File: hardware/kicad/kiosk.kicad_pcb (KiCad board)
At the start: 2 copper layers, 158 x 121 mm, 20 parts, among them J10 TerminalBlock_MaiXu_MX126-5.0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, J11 TerminalBlock_MaiXu_MX126-5.0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, J13 PinHeader_1x09_P2.54mm_Vertic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, J14 PinHeader_1x04_P2.54mm_Vertic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, J3 PinSocket_1x14_P2.54mm_Vertic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, J4 PinSocket_1x06_P2.54mm_Vertic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, J5 PinSocket_1x04_P2.54mm_Vertic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, J6 PinSocket_1x06_P2.54mm_Vertic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, J7 PinSocket_1x07_P2.54mm_Vertic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, J9 PinHeader_1x03_P2.54mm_Vertic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, U1 ESP32-S3-CAM

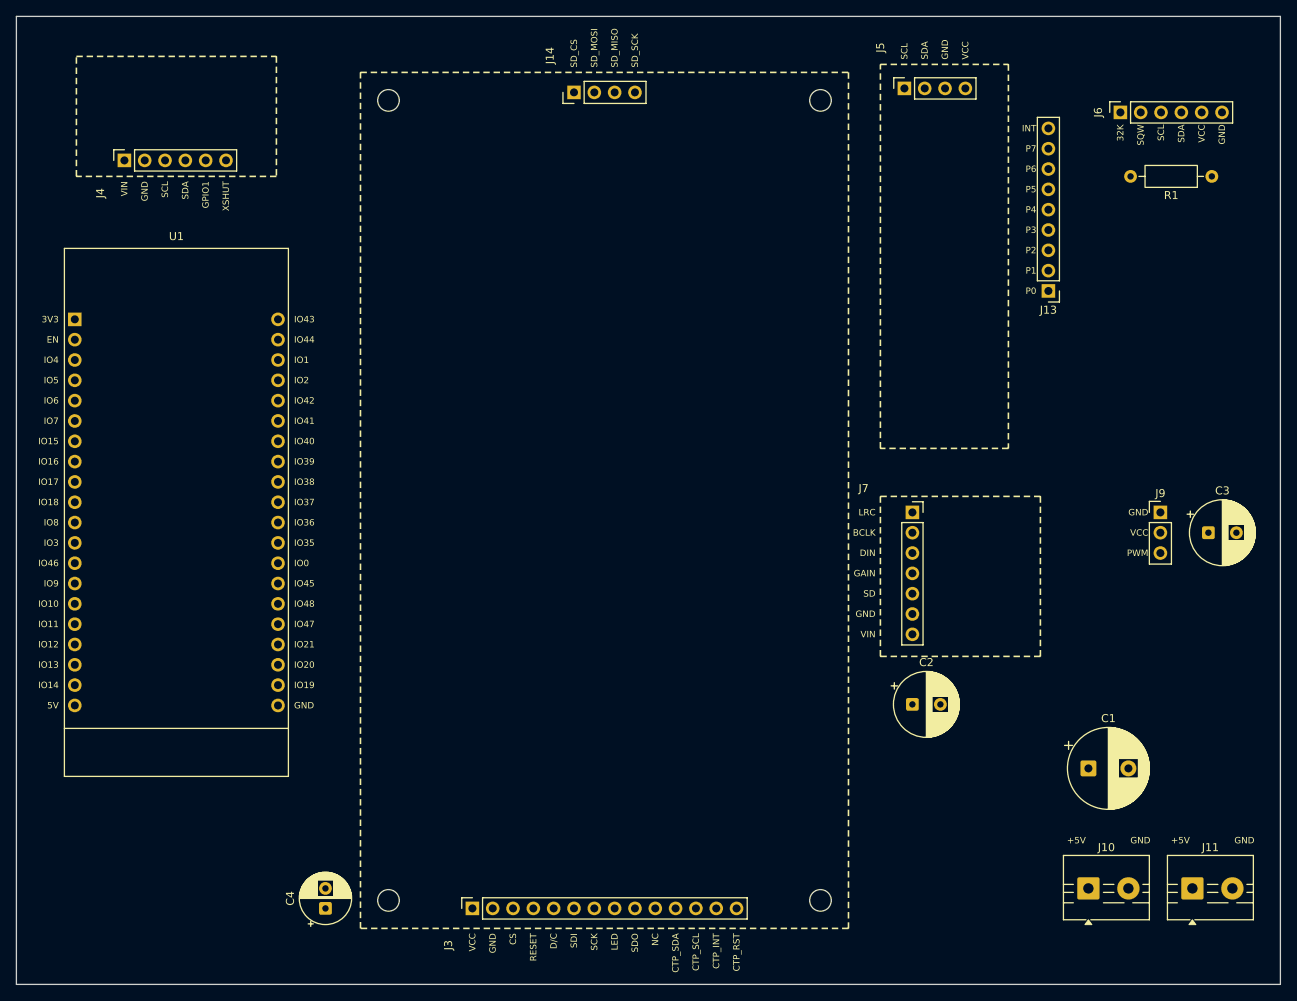
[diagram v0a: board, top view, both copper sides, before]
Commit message: fix(hardware): centre each socket across the module body it carries
J5's four-pin row sat 1.19 mm left of its outline's centre, so the
expander would have hung over one side of its own socket. J4 and J7 were
out by 0.15 and 0.38 for the same reason: the placements were typed to
land near the body rather than measured against it.

All four sockets under a module body are now centred along the axis their
row runs — J3 and J14 already were, because the panel rectangle is derived
from J3 rather than written down.

check_pcb gains the rule at a 0.3 mm tolerance, which is roughly where the
drift starts being visible against the dashed outline. Proven by putting
J5 back and watching it report -1.19.

Task: E14-T8
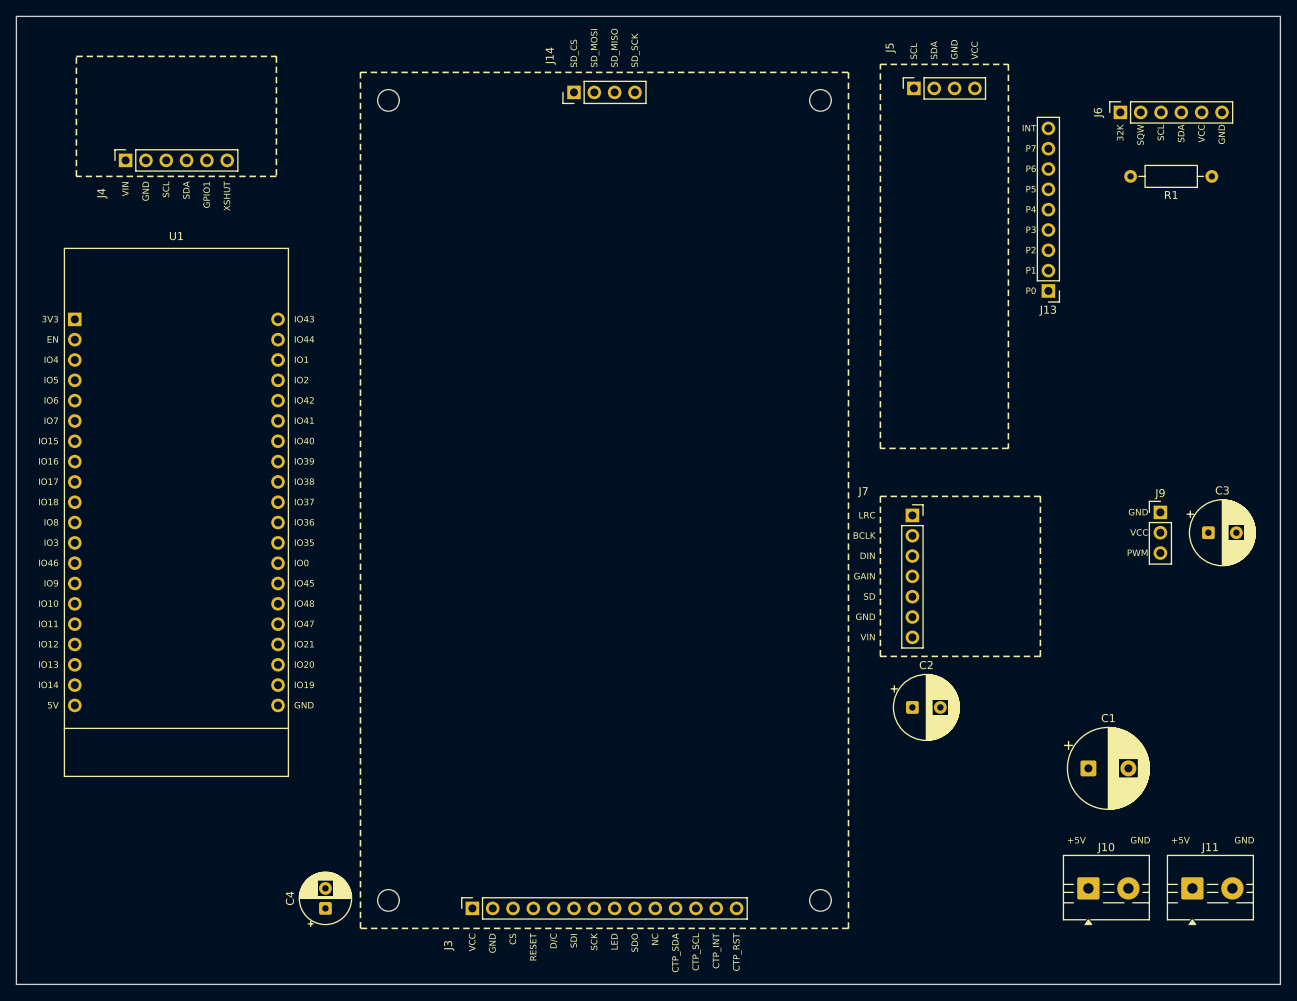
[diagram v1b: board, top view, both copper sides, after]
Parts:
- moved J5 1.19 mm to (112.2, 9.00)
- moved J7 0.38 mm to (112.0, 62.4)
- moved C2 0.38 mm to (112.0, 86.4)
- moved J4 0.15 mm to (13.7, 18.0)
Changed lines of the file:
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@@
 	(footprint "Connector_PinSocket_2.54mm:PinSocket_1x07_P2.54mm_Vertical"
 		(layer "F.Cu")
-		(at 112 62)
+		(at 112 62.38)
 		(descr "Through hole straight socket strip, 1x07, 2.54mm pitch, single row (from Kicad 4.0.7), script generated")
 		(tags "Through hole socket strip THT 1x07 2.54mm single row")
@@
 	(footprint "Connector_PinSocket_2.54mm:PinSocket_1x04_P2.54mm_Vertical"
 		(layer "F.Cu")
-		(at 111 9 90)
+		(at 112.19 9 90)
 		(descr "Through hole straight socket strip, 1x04, 2.54mm pitch, single row (from Kicad 4.0.7), script generated")
 		(tags "Through hole socket strip THT 1x04 2.54mm single row")
@@
 	(footprint "Connector_PinSocket_2.54mm:PinSocket_1x06_P2.54mm_Vertical"
 		(layer "F.Cu")
-		(at 13.5 18 90)
+		(at 13.65 18 90)
 		(descr "Through hole straight socket strip, 1x06, 2.54mm pitch, single row (from Kicad 4.0.7), script generated")
 		(tags "Through hole socket strip THT 1x06 2.54mm single row")
@@
 	(footprint "Capacitor_THT:CP_Radial_D8.0mm_P3.50mm"
 		(layer "F.Cu")
-		(at 112 86)
+		(at 112 86.38)
 		(descr "CP, Radial series, Radial, pin pitch=3.50mm, diameter=8mm, height=12mm, Electrolytic Capacitor")
 		(tags "CP Radial series Radial pin pitch 3.50mm diameter 8mm height 12mm Electrolytic Capacitor")
@@
 	)
 	(gr_text "LRC"
-		(at 107.4 62 0)
+		(at 107.4 62.38 0)
 		(layer "F.SilkS")
 		(effects
@@
 	)
 	(gr_text "BCLK"
-		(at 107.4 64.54 0)
+		(at 107.4 64.92 0)
 		(layer "F.SilkS")
 		(effects
@@
 	)
 	(gr_text "DIN"
-		(at 107.4 67.08 0)
+		(at 107.4 67.46 0)
 		(layer "F.SilkS")
 		(effects
@@
 	)
 	(gr_text "GAIN"
-		(at 107.4 69.62 0)
+		(at 107.4 70 0)
 		(layer "F.SilkS")
 		(effects
@@
 	)
 	(gr_text "SD"
-		(at 107.4 72.16 0)
+		(at 107.4 72.54 0)
 		(layer "F.SilkS")
 		(effects
@@
 	)
 	(gr_text "GND"
-		(at 107.4 74.7 0)
+		(at 107.4 75.08 0)
 		(layer "F.SilkS")
 		(effects
@@
 	)
 	(gr_text "VIN"
-		(at 107.4 77.24 0)
+		(at 107.4 77.62 0)
 		(layer "F.SilkS")
 		(effects
@@
 	)
 	(gr_text "SCL"
-		(at 111 5.4 90)
+		(at 112.19 5.4 90)
 		(layer "F.SilkS")
 		(effects
@@
 	)
 	(gr_text "SDA"
-		(at 113.54 5.4 90)
+		(at 114.73 5.4 90)
 		(layer "F.SilkS")
 		(effects
@@
 	)
 	(gr_text "GND"
-		(at 116.08 5.4 90)
+		(at 117.27 5.4 90)
 		(layer "F.SilkS")
 		(effects
@@
 	)
 	(gr_text "VCC"
-		(at 118.62 5.4 90)
+		(at 119.81 5.4 90)
 		(layer "F.SilkS")
 		(effects
@@
 	)
 	(gr_text "VIN"
-		(at 13.5 20.6 90)
+		(at 13.65 20.6 90)
 		(layer "F.SilkS")
 		(effects
@@
 	)
 	(gr_text "GND"
-		(at 16.04 20.6 90)
+		(at 16.19 20.6 90)
 		(layer "F.SilkS")
 		(effects
@@
 	)
 	(gr_text "SCL"
-		(at 18.58 20.6 90)
+		(at 18.73 20.6 90)
 		(layer "F.SilkS")
 		(effects
@@
 	)
 	(gr_text "SDA"
-		(at 21.12 20.6 90)
+		(at 21.27 20.6 90)
 		(layer "F.SilkS")
 		(effects
@@
 	)
 	(gr_text "GPIO1"
-		(at 23.66 20.6 90)
+		(at 23.81 20.6 90)
 		(layer "F.SilkS")
 		(effects
@@
 	)
 	(gr_text "XSHUT"
-		(at 26.2 20.6 90)
+		(at 26.35 20.6 90)
 		(layer "F.SilkS")
 		(effects

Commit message: fix(hardware): set the three gaps around the panel equal
The panel sat 8.76 mm from the devkit and 3.99 mm from both the expander
and the amplifier outlines, so it read as pushed to the right of its own
row.

Halving the difference does not work: the left gap holds C4, whose can is
6.3 mm, and an even 6.38 mm gap leaves it 0.04 mm a side. So the panel
moves 1.46 mm left and the parts right of it move 1.85 mm right, which
lands all three gaps on 7.3 mm and keeps a quarter of a millimetre of
courtyard around the can. The board stays 158 wide because J9, C3, C1 and
the two terminals did not have to move with them.

The comment the previous commit added to gen_pcb.py used a word CI blocks
in comments; it is reworded here rather than left for the next run to trip
over.

Task: E14-T8
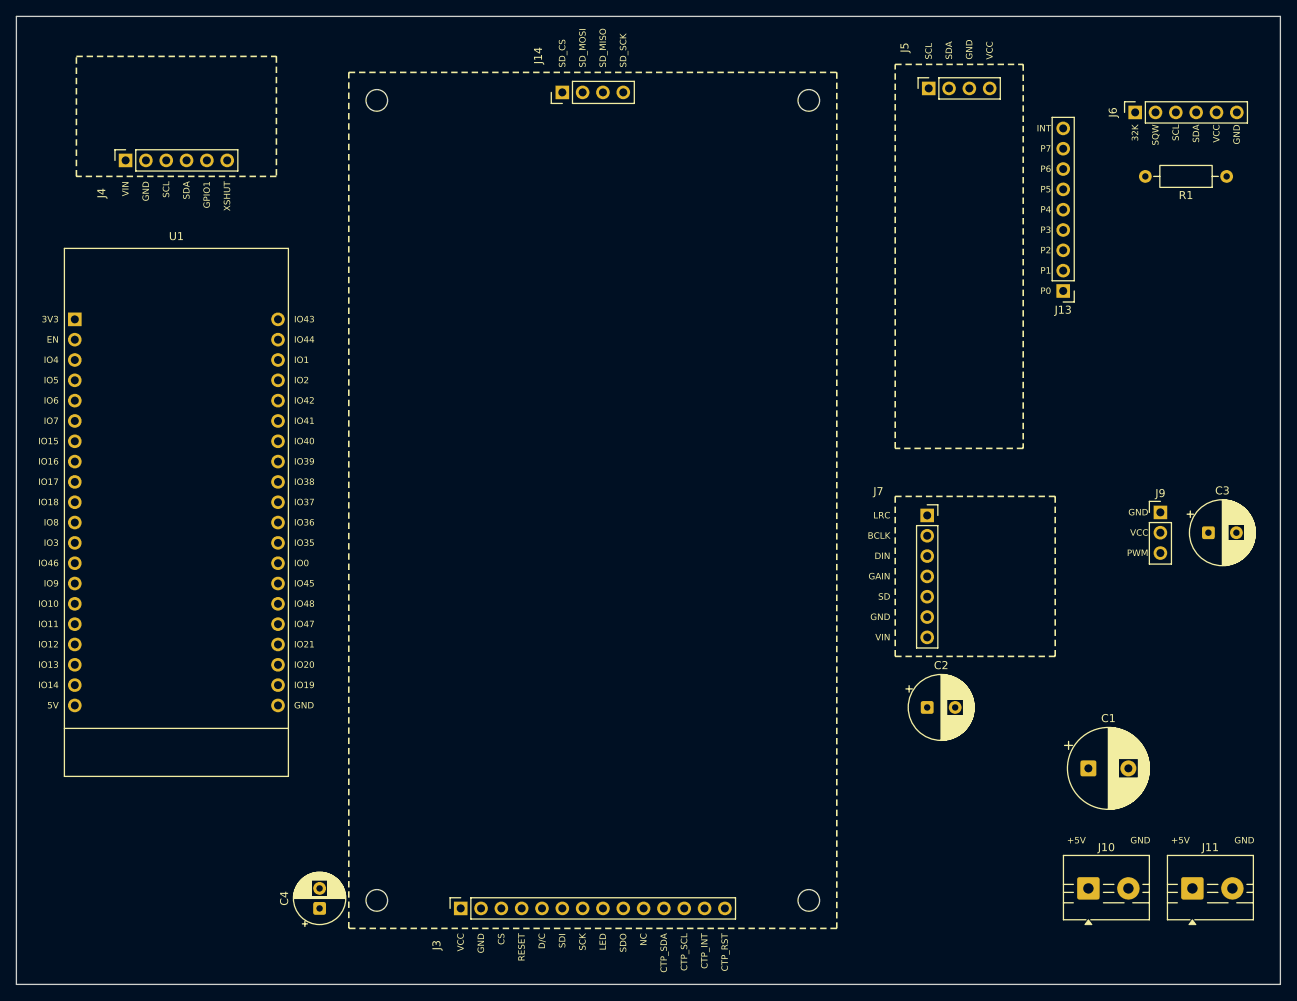
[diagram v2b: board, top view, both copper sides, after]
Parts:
- moved J5 1.85 mm to (114.0, 9.00)
- moved C2 1.85 mm to (113.8, 86.4)
- moved J13 1.85 mm to (130.8, 34.3)
- moved J6 1.85 mm to (139.8, 12.0)
- moved J7 1.85 mm to (113.8, 62.4)
- moved R1 1.85 mm to (151.3, 20.0)
- moved H2 1.46 mm to (99.0, 10.5)
- moved H3 1.46 mm to (99.0, 110.5)
- moved J14 1.46 mm to (68.2, 9.50)
- moved H1 1.46 mm to (45.0, 10.5)
- moved H4 1.46 mm to (45.0, 110.5)
- moved J3 1.46 mm to (55.5, 111.5)
- moved C4 0.73 mm to (37.9, 111.5)

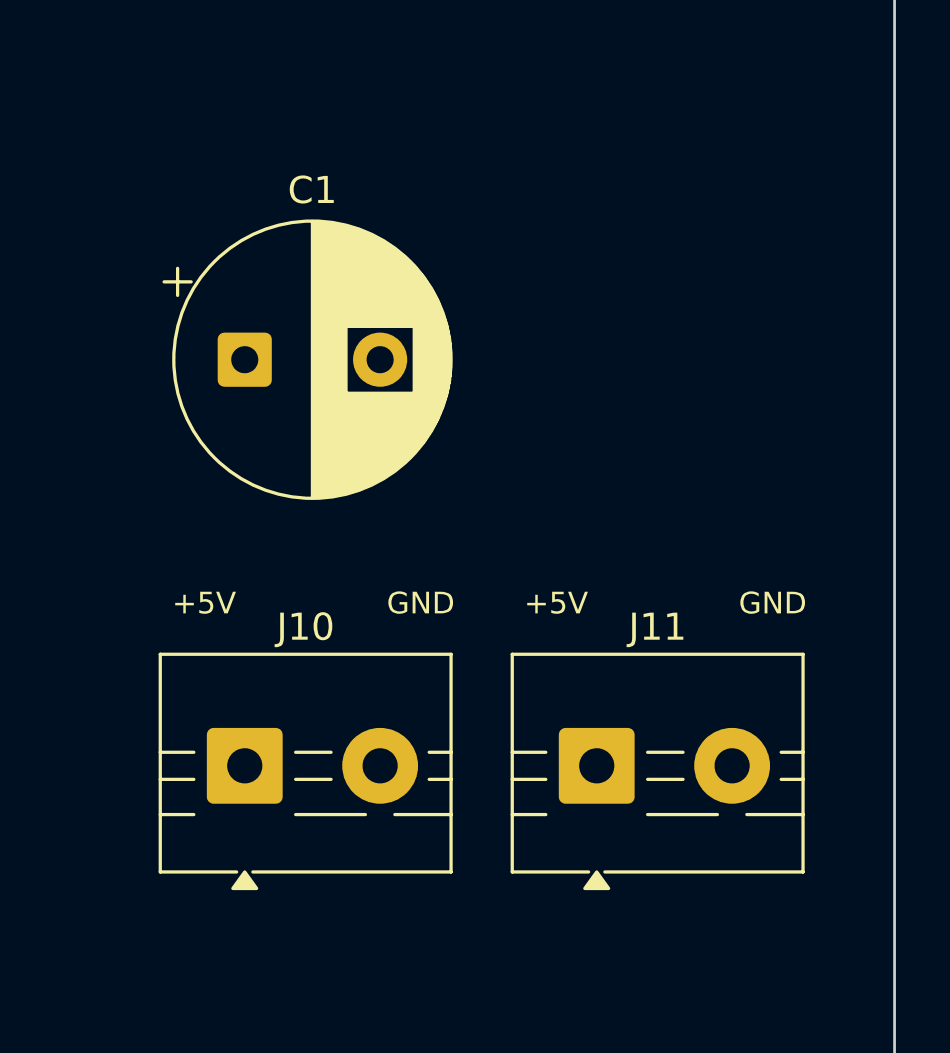
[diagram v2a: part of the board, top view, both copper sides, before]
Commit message: fix(hardware): put the two supply terminals in step and centre C1 on them
The four screws ran at 5.0, 8.0, 5.0 mm. The 8 was not a decision — it is
what was left when J11 moved inward to trim the board — and an uneven row
of identical terminals reads as a mistake. They now sit as close as their
courtyards allow, which is 6.5 mm, so the row goes 5.0, 6.5, 5.0 and the
two outlines touch rather than overlap.

That also makes rule 1 of section 2.5 nearly literal: J10.GND to J11.GND
is 11.5 mm, from 13.0.

C1 was aligned over J10 alone, leaving J11 outside the group. It is the
bulk store for the point where the two grounds meet, not for one terminal,
so it now centres across all four screws.

Task: E14-T8
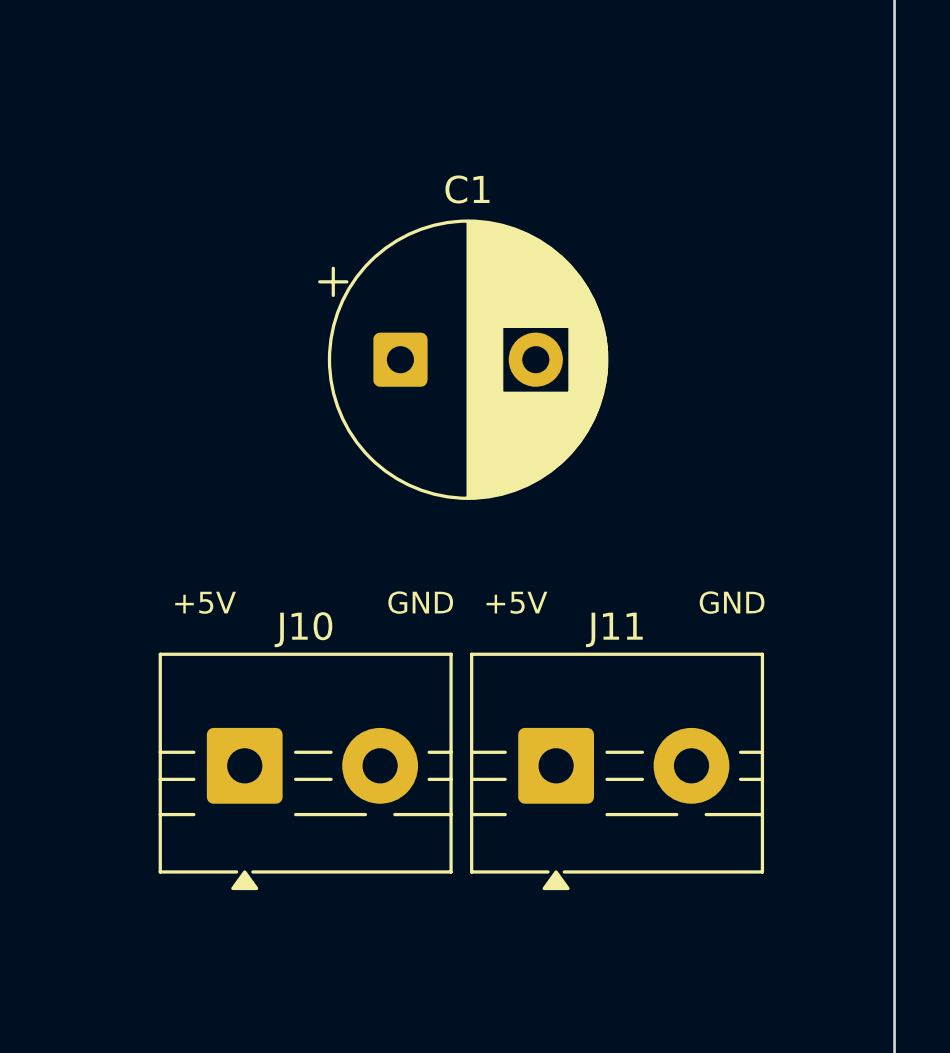
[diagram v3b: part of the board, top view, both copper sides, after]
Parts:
- moved C1 5.75 mm to (139.8, 94.0)
- moved J11 1.50 mm to (145.5, 109.0)
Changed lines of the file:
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@@
 	(footprint "TerminalBlock:TerminalBlock_MaiXu_MX126-5.0-02P_1x02_P5.00mm"
 		(layer "F.Cu")
-		(at 147 109)
+		(at 145.5 109)
 		(descr "terminal block MaiXu MX126-5.0-02P, 2 pins, pitch 5mm, size 10.5x7.8mm, drill diameter 1.3mm, pad diameter 2.8mm, https://www.lcsc.com/datasheet/lcsc_datasheet_2309150913_MAX-MX126-5-0-03P-GN01-Cu-S-A_C5188435.pdf")
 		(tags "THT terminal block MaiXu MX126-5.0-02P pitch 5mm size 10.5x7.8mm drill 1.3mm pad 2.8mm")
@@
 	(footprint "Capacitor_THT:CP_Radial_D10.0mm_P5.00mm"
 		(layer "F.Cu")
-		(at 134 94)
+		(at 139.75 94)
 		(descr "CP, Radial series, Radial, pin pitch=5.00mm, diameter=10mm, height=16mm, Electrolytic Capacitor")
 		(tags "CP Radial series Radial pin pitch 5.00mm diameter 10mm height 16mm Electrolytic Capacitor")
@@
 	)
 	(gr_text "+5V"
-		(at 145.5 103 0)
+		(at 144 103 0)
 		(layer "F.SilkS")
 		(effects
@@
 	)
 	(gr_text "GND"
-		(at 153.5 103 0)
+		(at 152 103 0)
 		(layer "F.SilkS")
 		(effects
